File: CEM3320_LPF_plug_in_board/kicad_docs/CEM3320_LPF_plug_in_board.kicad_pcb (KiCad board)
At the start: 2 copper layers, 58.4 x 50.8 mm, 42 parts, among them J1 signal_in, J2 signal_in, J3 signal_out, J4 Conn_01x08_Male, U1 CEM3320, U2 TL072

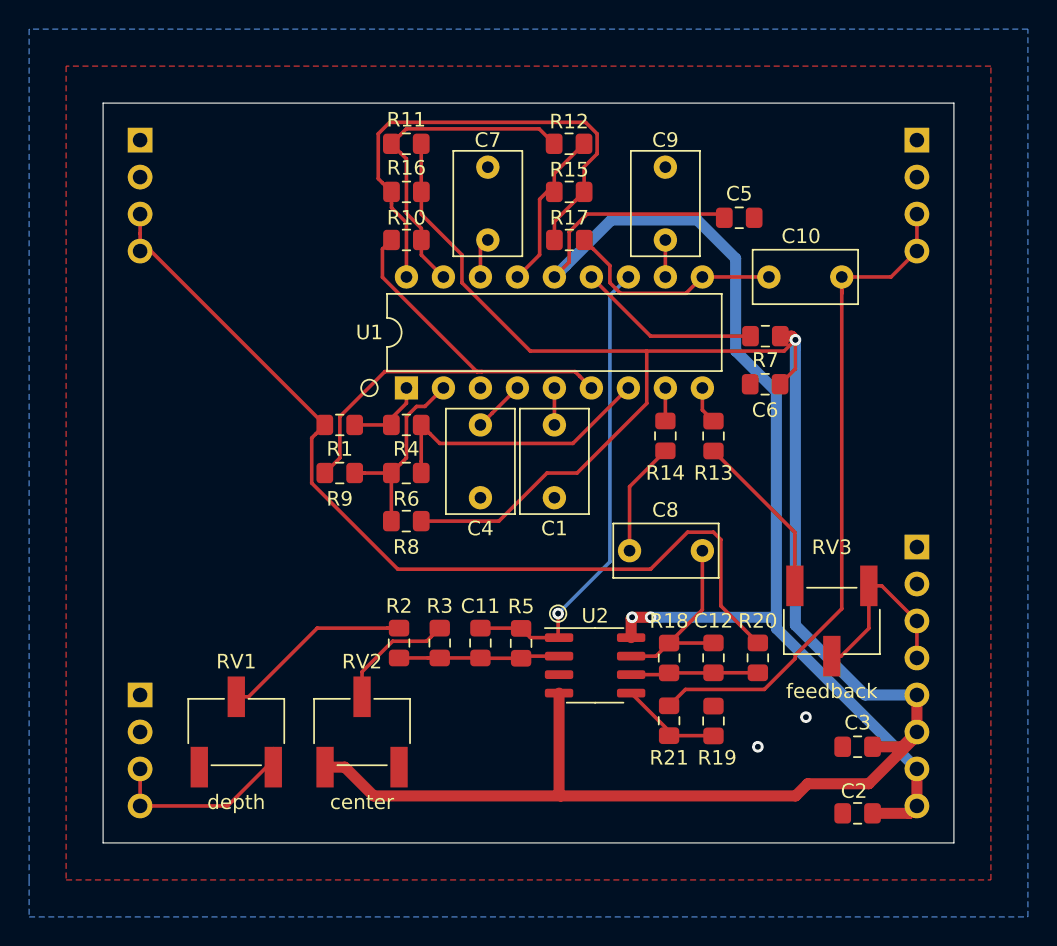
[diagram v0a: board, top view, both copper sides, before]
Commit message: clean up CEM3320 LPF, add smd cap footprints for timing caps
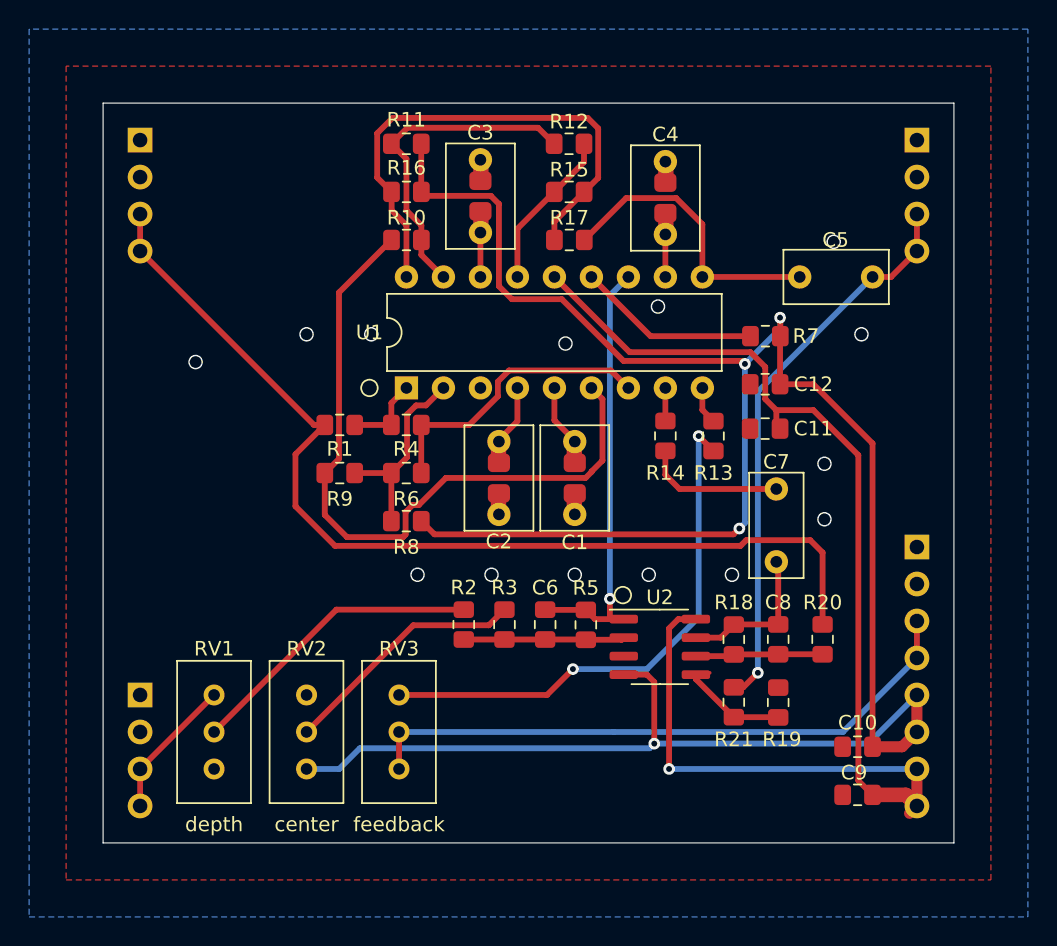
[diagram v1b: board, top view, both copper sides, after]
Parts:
- removed the C10 at (177.7, 88.1)
- removed the C8 at (168.1, 106.9)
- removed the C9 at (165.6, 85.6)
- added C2: 220pF, cem3320:timing_cap_dual_fp, F.Cu at (154.2, 99.4)
- added C3: 220pF, cem3320:timing_cap_dual_fp, F.Cu at (152.9, 85.1)
- added C5: 470nF, Capacitor_THT:C_Rect_L7.0mm_W3.5mm_P5.00mm, F.Cu at (179.8, 88.1)
- C1, C4: footprint Capacitor_THT:C_Rect_L7.0mm_W4.5mm_P5.00mm -> cem3320:timing_cap_dual_fp
- C7: value 220pF -> 470nF; footprint Capacitor_THT:C_Rect_L7.0mm_W4.5mm_P5.00mm -> Capacitor_THT:C_Rect_L7.0mm_W3.5mm_P5.00mm
- J1: value signal_in -> cutoff_CV_in
- J4: value Conn_01x08_Male -> feedback_CV_in_and_PS
- RV1, RV2, RV3: footprint Potentiometer_SMD:Potentiometer_Bourns_3269W_Vertical -> Potentiometer_THT:Potentiometer_Bourns_3296W_Vertical
- moved RV3 31.4 mm to (147.3, 121.9), turned to 270 degrees
- moved C7 29.7 mm to (173.2, 107.7)
- moved C4 18.2 mm to (165.6, 85.2), turned to 90 degrees
- moved C11 14.6 mm to (172.5, 98.6), turned to 180 degrees
- moved C6 4.62 mm to (157.4, 112.0)
- moved R2 4.62 mm to (151.8, 112.0)
- moved R3 4.62 mm to (154.6, 112.0)
- moved R5 4.62 mm to (160.1, 112.0)
- moved U2 4.62 mm to (165.2, 113.5)
- moved C8 4.62 mm to (173.4, 113.0)
- moved R18 4.62 mm to (170.3, 113.0)
- moved R19 4.62 mm to (173.4, 117.4)
- moved R20 4.62 mm to (176.4, 113.0)
- moved R21 4.62 mm to (170.3, 117.3)
- moved RV2 4.58 mm to (141.0, 121.9), turned to 270 degrees
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- renumbered C3 to C10, C5 to C11, C6 to C12, C11 to C6, C12 to C8, C2 to C9
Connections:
- C7 pad 2: GND -> Net-(C7-Pad2)
- C8 pad 1: Net-(C12-Pad1) -> Net-(C7-Pad1)
- R14 pad 1: Net-(C8-Pad2) (its old number) -> Net-(C7-Pad2)
- R18 pad 1: Net-(C12-Pad1) -> Net-(C7-Pad1)
- U1 pad 11: Net-(C9-Pad1) -> Net-(C4-Pad1)
- U1 pad 16: Net-(C7-Pad1) -> Net-(C3-Pad1)
- U1 pad 4: Net-(C4-Pad1) -> Net-(C2-Pad1)
- U2 pad 7: Net-(C12-Pad1) -> Net-(C7-Pad1)
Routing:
- net Net-(J4-Pad3): track 13.1 -> 42.7 mm
- net Net-(R13-Pad2): track 11.6 -> 36.7 mm, vias 0 -> 2
- net Net-(R10-Pad2): track 35.7 -> 48.9 mm
- net Net-(C12-Pad1): track 13.1 -> 0.00 mm
- net -12V: track 149.4 -> 162.1 mm, vias 1 -> 4
- net Net-(C7-Pad2): track 0.00 -> 9.67 mm
- net Net-(R3-Pad1): track 8.29 -> 17.1 mm
- net /wet: track 47.1 -> 38.8 mm, vias 0 -> 1
- net Net-(C8-Pad2) (its old number): track 7.88 -> 0.00 mm
- net Net-(C7-Pad1): track 2.75 -> 10.4 mm
- net Net-(R2-Pad2): track 13.1 -> 20.6 mm
- net GND: track 0.00 -> 5.74 mm, vias 2 -> 14
- net Net-(C2-Pad1): track 0.00 -> 5.60 mm
- net Net-(C5-Pad2): track 15.4 -> 20.3 mm
- net /dry: track 64.5 -> 69.4 mm
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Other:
- board text added: "CEM3320_LPF_plug_in_board rev1.1 2019-06-09"
- board text removed: "CEM3320_LPF_plug_in_board rev1.0 2019-06-09"

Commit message: swap j2 and j1 positions for consistency
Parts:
- renumbered J2 to J1, J1 to J2
